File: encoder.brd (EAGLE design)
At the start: 22.8 x 32.7 mm, 3 parts

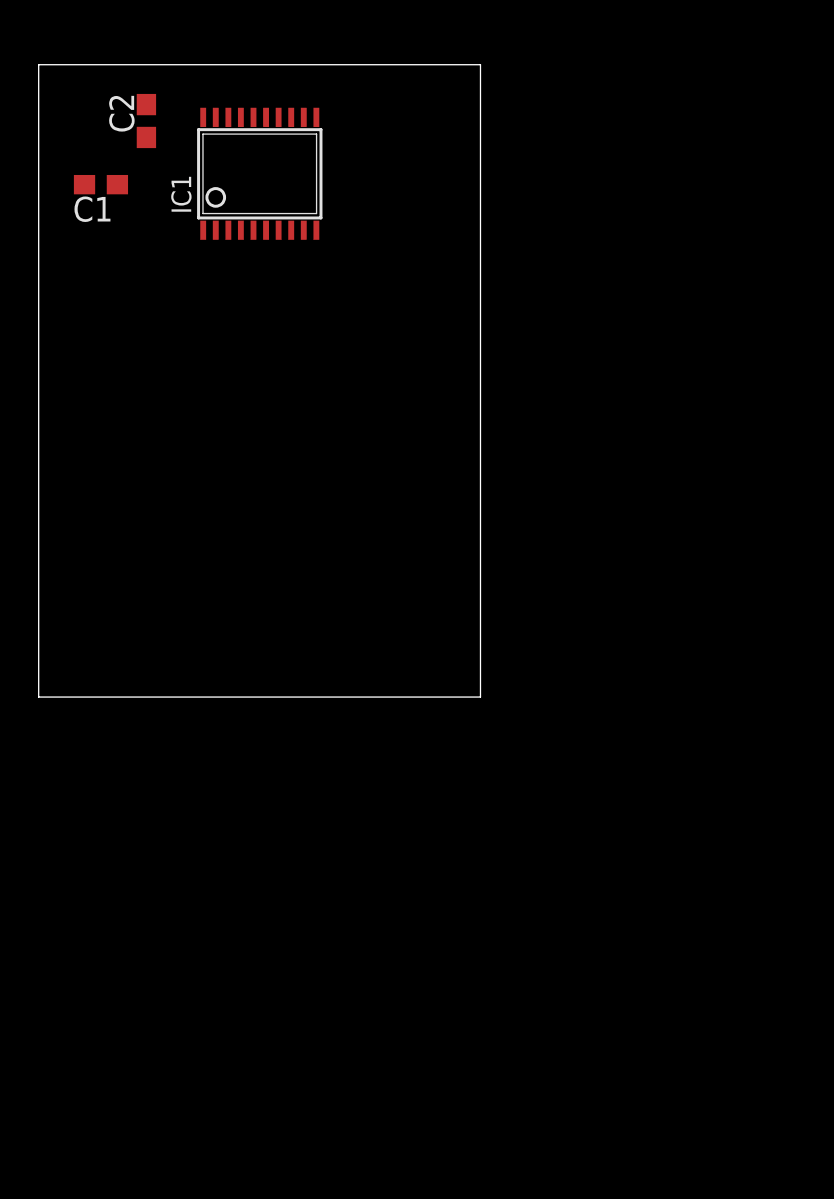
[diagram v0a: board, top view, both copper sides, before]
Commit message: pcb do enkoderow i poprawione lbr
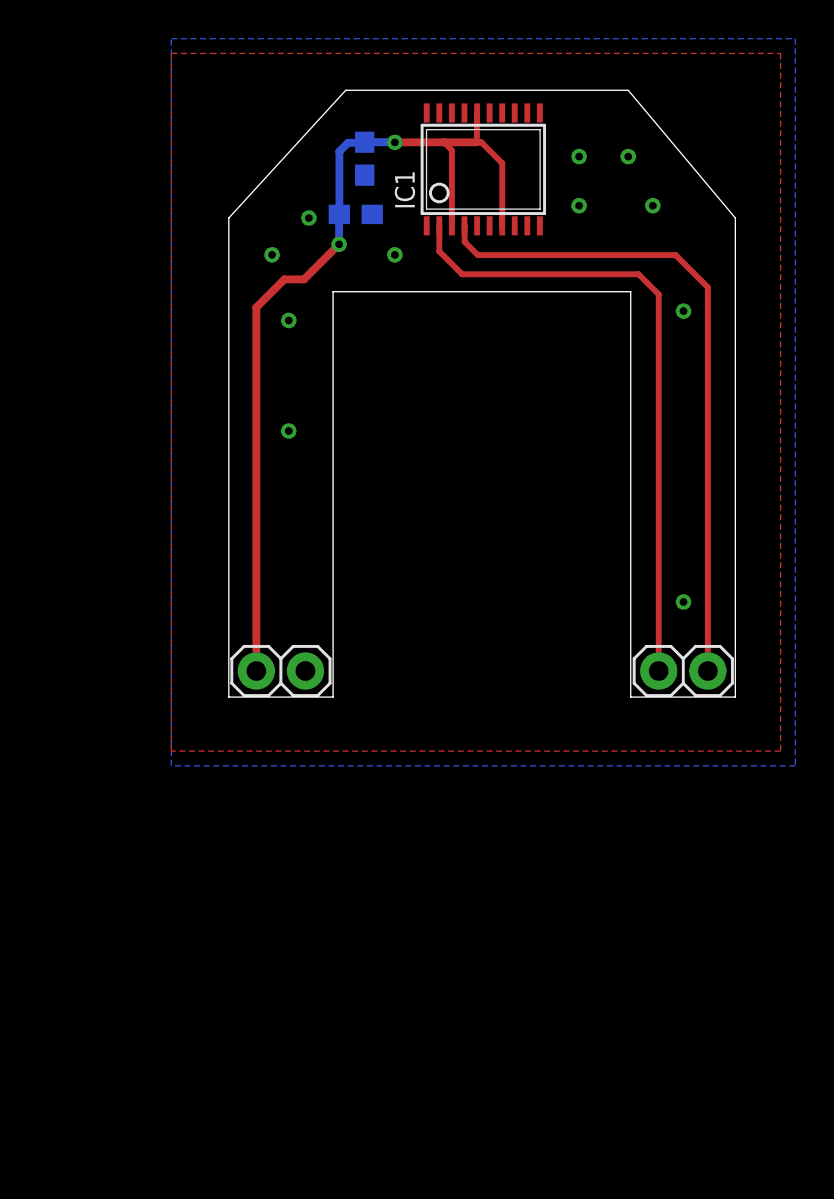
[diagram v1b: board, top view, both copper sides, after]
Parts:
- added JP1, JP2: PINHD_1X2_ROUND, _microMouse:PINHD_1X2_ROUND
- moved C1 13.7 mm to (16.9, 27.8), flipped to the bottom, turned to 270 degrees
- moved C2 11.9 mm to (16.4, 25.0), flipped to the bottom, turned to 180 degrees
- moved IC1 11.6 mm to (23.0, 27.3)
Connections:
- net CHA: now also JP2.1
- net CHB: now also JP2.2
- net GND: now also JP1.2
- net VCC: now also JP1.1
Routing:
- net VCC: track 0.00 -> 47.5 mm, vias 0 -> 2
- net CHB: track 0.00 -> 34.2 mm
- net CHA: track 0.00 -> 33.1 mm
- added copper zone on layer 1, net GND
- added copper zone on layer 16, net GND
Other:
- board size 22.8 x 32.7 mm -> 26.2 x 31.4 mm
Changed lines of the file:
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@@
 <setting verticaltext="up"/>
 </settings>
-<grid distance="1" unitdist="mm" unit="mm" style="lines" multiple="1" display="yes" altdistance="0.025" altunitdist="inch" altunit="inch"/>
+<grid distance="10" unitdist="mil" unit="mil" style="lines" multiple="1" display="yes" altdistance="1" altunitdist="mil" altunit="mil"/>
 <layers>
 <layer number="1" name="Top" color="4" fill="1" visible="yes" active="yes"/>
@@
 <board>
 <plain>
-<wire x1="0" y1="0" x2="22.84" y2="0" width="0" layer="20"/>
-<wire x1="22.84" y1="0" x2="22.84" y2="32.69" width="0" layer="20"/>
-<wire x1="22.84" y1="32.69" x2="0" y2="32.69" width="0" layer="20"/>
-<wire x1="0" y1="32.69" x2="0" y2="0" width="0" layer="20"/>
+<wire x1="9.8298" y1="0" x2="15.22" y2="0" width="0" layer="20"/>
+<wire x1="15.22" y1="0" x2="15.22" y2="20.9552" width="0" layer="20"/>
+<wire x1="15.22" y1="20.9552" x2="30.607" y2="20.9552" width="0" layer="20"/>
+<wire x1="30.607" y1="20.9552" x2="30.607" y2="0" width="0" layer="20"/>
+<wire x1="30.607" y1="0" x2="36.0172" y2="0" width="0" layer="20"/>
+<wire x1="36.0172" y1="0" x2="36.0172" y2="24.765" width="0" layer="20"/>
+<wire x1="36.0172" y1="24.765" x2="30.48" y2="31.369" width="0" layer="20"/>
+<wire x1="30.48" y1="31.369" x2="15.875" y2="31.369" width="0" layer="20"/>
+<wire x1="15.875" y1="31.369" x2="9.8298" y2="24.765" width="0" layer="20"/>
+<wire x1="9.8298" y1="24.765" x2="9.8298" y2="0" width="0" layer="20"/>
 </plain>
 <attributes>
@@
 </class>
 </classes>
-<designrules name="default">
+<designrules name="default *">
 <description language="de">&lt;b&gt;EAGLE Design Rules&lt;/b&gt;
 &lt;p&gt;
@@
 <param name="mdViaViaSameLayer" value="8mil"/>
 <param name="mnLayersViaInSmd" value="2"/>
-<param name="mdCopperDimension" value="40mil"/>
+<param name="mdCopperDimension" value="30mil"/>
 <param name="mdDrill" value="8mil"/>
 <param name="mdSmdStop" value="0mil"/>
@@
 <param name="srMinRoundness" value="0mil"/>
 <param name="srMaxRoundness" value="0mil"/>
-<param name="slThermalIsolate" value="10mil"/>
+<param name="slThermalIsolate" value="8mil"/>
 <param name="slThermalsForVias" value="0"/>
 <param name="dpMaxLengthDifference" value="10mm"/>
@@
 </autorouter>
 <elements>
-<element name="C1" library="rcl" package="C0603" value="10u" x="3.22" y="26.49" rot="R180"/>
-<element name="C2" library="rcl" package="C0603" value="100n" x="5.57" y="29.78" rot="R90"/>
-<element name="IC1" library="_microMouse" package="TSSOP20" value="" x="11.43" y="27.05"/>
+<element name="C1" library="rcl" package="C0603" value="10u" x="16.854" y="27.8326" rot="MR270"/>
+<element name="C2" library="rcl" package="C0603" value="100n" x="16.3942" y="24.9502" rot="MR180"/>
+<element name="IC1" library="_microMouse" package="TSSOP20" value="" x="22.987" y="27.2786"/>
+<element name="JP1" library="_microMouse" package="PINHD_1X2_ROUND" value="PINHD_1X2_ROUND" x="13.7922" y="1.3462"/>
+<element name="JP2" library="_microMouse" package="PINHD_1X2_ROUND" value="PINHD_1X2_ROUND" x="34.5948" y="1.3462"/>
 </elements>
 <signals>
@@
 <contactref element="C1" pad="2"/>
 <contactref element="C2" pad="2"/>
-<wire x1="8.505" y1="29.9678" x2="8.505" y2="24.1322" width="0" layer="19" extent="1-1"/>
-<wire x1="11.755" y1="29.9678" x2="8.505" y2="29.9678" width="0" layer="19" extent="1-1"/>
-<wire x1="5.57" y1="30.63" x2="11.755" y2="29.9678" width="0" layer="19" extent="1-1"/>
-<wire x1="2.37" y1="26.49" x2="5.57" y2="30.63" width="0" layer="19" extent="1-1"/>
+<contactref element="JP1" pad="2"/>
+<via x="12.065" y="22.86" extent="1-16" drill="0.4"/>
+<via x="13.97" y="24.765" extent="1-16" drill="0.4"/>
+<via x="18.415" y="22.86" extent="1-16" drill="0.4"/>
+<via x="27.94" y="25.4" extent="1-16" drill="0.4"/>
+<via x="31.75" y="25.4" extent="1-16" drill="0.4"/>
+<via x="30.48" y="27.94" extent="1-16" drill="0.4"/>
+<via x="27.94" y="27.94" extent="1-16" drill="0.4"/>
+<via x="33.3375" y="19.9517" extent="1-16" drill="0.4"/>
+<via x="33.3375" y="4.9149" extent="1-16" drill="0.4"/>
+<via x="12.9286" y="13.7541" extent="1-16" drill="0.4"/>
+<via x="12.9286" y="19.4691" extent="1-16" drill="0.4"/>
+<polygon width="0.3048" layer="1" isolate="0.254">
+<vertex x="8.89" y="33.274"/>
+<vertex x="38.354" y="33.274"/>
+<vertex x="38.354" y="-2.794"/>
+<vertex x="6.858" y="-2.794"/>
+<vertex x="6.858" y="33.274"/>
+</polygon>
+<polygon width="0.4064" layer="16" spacing="0.6096" isolate="0.3048">
+<vertex x="6.858" y="34.036"/>
+<vertex x="39.116" y="34.036"/>
+<vertex x="39.116" y="-3.556"/>
+<vertex x="6.858" y="-3.556"/>
+</polygon>
 </signal>
 <signal name="CHA">
 <contactref element="IC1" pad="A"/>
+<contactref element="JP2" pad="1"/>
+<wire x1="20.712" y1="24.3608" x2="20.7137" y2="24.3591" width="0.3048" layer="1"/>
+<wire x1="20.7137" y1="24.3591" x2="20.7137" y2="23.0378" width="0.3048" layer="1"/>
+<wire x1="20.7137" y1="23.0378" x2="21.8948" y2="21.8567" width="0.3048" layer="1"/>
+<wire x1="21.8948" y1="21.8567" x2="31.0134" y2="21.8567" width="0.3048" layer="1"/>
+<wire x1="31.0134" y1="21.8567" x2="32.0548" y2="20.8153" width="0.3048" layer="1"/>
+<wire x1="32.0548" y1="20.8153" x2="32.0548" y2="1.3462" width="0.3048" layer="1"/>
 </signal>
 <signal name="CHB">
 <contactref element="IC1" pad="B"/>
+<contactref element="JP2" pad="2"/>
+<wire x1="22.012" y1="24.3608" x2="22.0218" y2="24.351" width="0.3048" layer="1"/>
+<wire x1="22.0218" y1="24.351" x2="22.0218" y2="23.5331" width="0.3048" layer="1"/>
+<wire x1="22.0218" y1="23.5331" x2="22.7076" y2="22.8473" width="0.3048" layer="1"/>
+<wire x1="22.7076" y1="22.8473" x2="32.9311" y2="22.8473" width="0.3048" layer="1"/>
+<wire x1="32.9311" y1="22.8473" x2="34.5948" y2="21.1836" width="0.3048" layer="1"/>
+<wire x1="34.5948" y1="21.1836" x2="34.5948" y2="1.3462" width="0.3048" layer="1"/>
 </signal>
 <signal name="VCC">
@@
 <contactref element="C1" pad="1"/>
 <contactref element="C2" pad="1"/>
-<wire x1="12.405" y1="24.1322" x2="9.805" y2="24.1322" width="0" layer="19" extent="1-1"/>
-<wire x1="11.105" y1="29.9678" x2="9.805" y2="24.1322" width="0" layer="19" extent="1-1"/>
-<wire x1="5.57" y1="28.93" x2="11.105" y2="29.9678" width="0" layer="19" extent="1-1"/>
-<wire x1="4.07" y1="26.49" x2="5.57" y2="28.93" width="0" layer="19" extent="1-1"/>
+<contactref element="JP1" pad="1"/>
+<wire x1="16.854" y1="28.6826" x2="18.415" y2="28.6826" width="0.4064" layer="16"/>
+<wire x1="18.415" y1="28.6826" x2="18.415" y2="28.6766" width="0.3048" layer="16"/>
+<via x="18.415" y="28.6766" extent="1-16" drill="0.4"/>
+<wire x1="18.415" y1="28.6766" x2="20.955" y2="28.6766" width="0.4064" layer="1"/>
+<wire x1="20.955" y1="28.6766" x2="22.6568" y2="28.6766" width="0.4064" layer="1"/>
+<wire x1="22.6568" y1="28.6766" x2="22.8854" y2="28.6766" width="0.3048" layer="1"/>
+<wire x1="22.6568" y1="30.1912" x2="22.662" y2="30.1964" width="0.3048" layer="1"/>
+<wire x1="21.362" y1="24.3608" x2="21.362" y2="28.2696" width="0.3048" layer="1"/>
+<wire x1="21.362" y1="28.2696" x2="20.955" y2="28.6766" width="0.3048" layer="1"/>
+<wire x1="23.962" y1="24.3608" x2="23.9649" y2="24.3608" width="0.3048" layer="1"/>
+<wire x1="23.9649" y1="24.3608" x2="23.9649" y2="27.5971" width="0.3048" layer="1"/>
+<wire x1="23.9649" y1="27.5971" x2="22.8854" y2="28.6766" width="0.3048" layer="1"/>
+<wire x1="22.6568" y1="30.1912" x2="22.6568" y2="28.6766" width="0.3048" layer="1"/>
+<wire x1="16.854" y1="28.6826" x2="16.8226" y2="28.6512" width="0.3048" layer="16"/>
+<wire x1="16.8226" y1="28.6512" x2="15.9893" y2="28.6512" width="0.4064" layer="16"/>
+<wire x1="15.9893" y1="28.6512" x2="15.5442" y2="28.2061" width="0.4064" layer="16"/>
+<wire x1="15.5442" y1="28.2061" x2="15.5442" y2="24.9502" width="0.4064" layer="16"/>
+<wire x1="15.5442" y1="24.9502" x2="15.5321" y2="24.9381" width="0.3048" layer="16"/>
+<wire x1="15.5321" y1="24.9381" x2="15.5321" y2="23.4061" width="0.4064" layer="16"/>
+<via x="15.5321" y="23.4061" extent="1-16" drill="0.4"/>
+<wire x1="15.5321" y1="23.4061" x2="13.716" y2="21.59" width="0.4064" layer="1"/>
+<wire x1="13.716" y1="21.59" x2="12.7" y2="21.59" width="0.4064" layer="1"/>
+<wire x1="12.7" y1="21.59" x2="11.2522" y2="20.1422" width="0.4064" layer="1"/>
+<wire x1="11.2522" y1="20.1422" x2="11.2522" y2="1.3462" width="0.4064" layer="1"/>
 </signal>
 </signals>
